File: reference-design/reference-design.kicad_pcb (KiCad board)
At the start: 2 copper layers, 104 x 83.9 mm, 31 parts

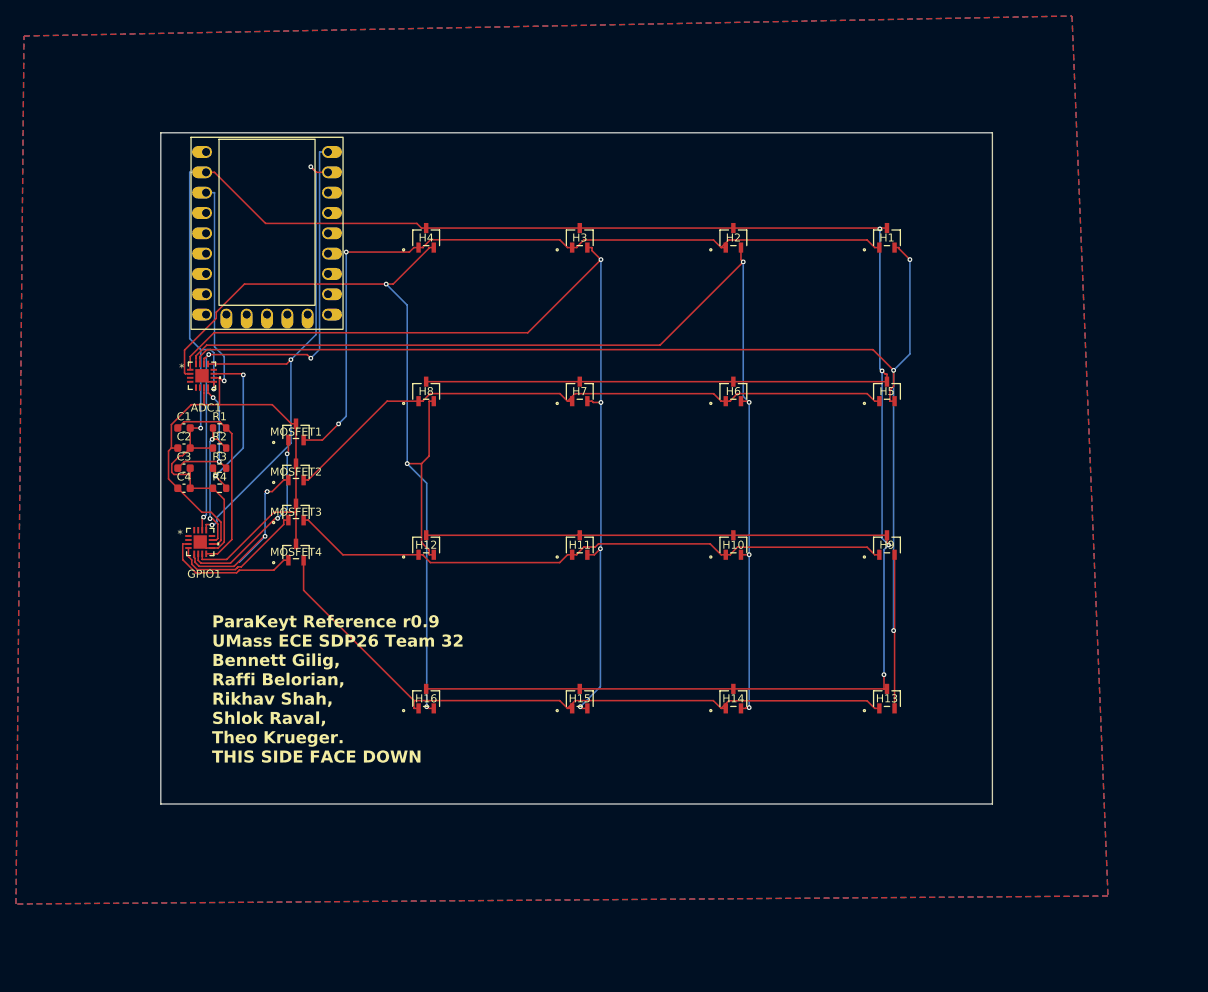
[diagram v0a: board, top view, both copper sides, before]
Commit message: add rp2040 cutout and keyswitch outlines
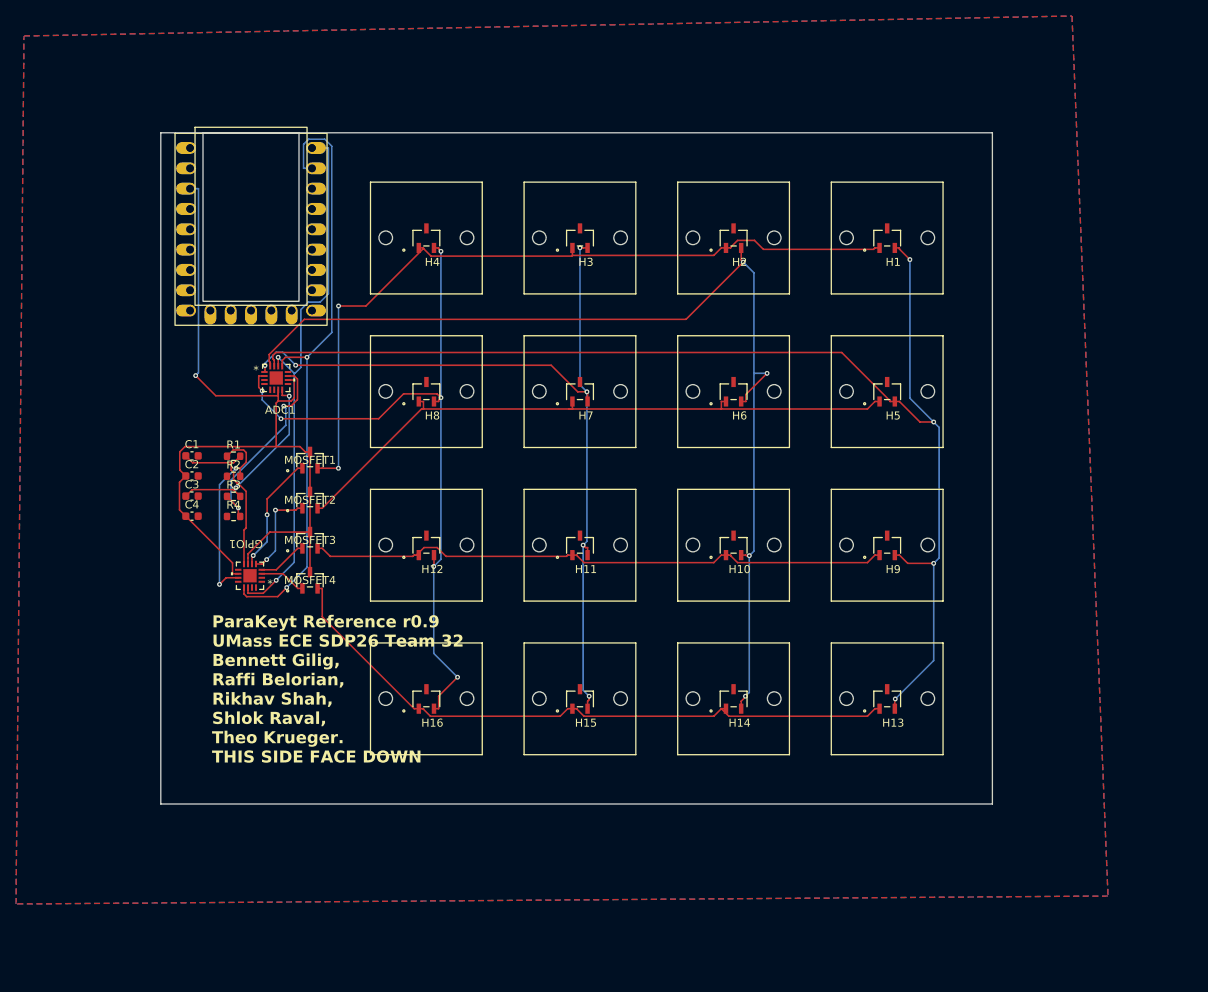
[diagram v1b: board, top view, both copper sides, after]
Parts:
- H1, H10, H11, H12, H13, H14, H15, H16, H2, H3, H4, H5, H6, H7, H8, H9: footprint AH49FNTR_G1:SC59_DIO -> AH49FNTR_G1:SC59_DIO_KeyswitchOutline_NoRuleArea
- moved ADC1 9.28 mm to (26.5, 42.8)
- moved GPIO1 7.52 mm to (23.2, 67.5), turned to 180 degrees
- moved MOSFET4 3.94 mm to (30.8, 68.0)
- moved MOSFET3 3.94 mm to (30.8, 63.0)
- moved R1 3.94 mm to (21.2, 52.5)
- moved R2 3.94 mm to (21.2, 55.0)
- moved R4 3.94 mm to (21.2, 60.1)
- moved MOSFET1 3.94 mm to (30.8, 53.0)
- moved MOSFET2 3.94 mm to (30.8, 58.0)
- moved R3 3.94 mm to (21.2, 57.5)
- moved C1 3.63 mm to (16.0, 52.5)
- moved C2 3.63 mm to (16.0, 55.0)
- moved C4 3.63 mm to (16.0, 60.0)
- moved C3 3.63 mm to (16.0, 57.5)
- moved MCU1 2.06 mm to (23.4, 24.2)
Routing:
- net GND: track 395.8 -> 0.00 mm, vias 6 -> 0
- net col3: track 119.4 -> 92.8 mm, vias 3 -> 6
- net row1: track 30.7 -> 11.7 mm
- net col2: track 122.2 -> 106.4 mm, vias 4 -> 6
- net row3: track 17.3 -> 5.84 mm
- net i2c0_scl: track 65.0 -> 76.4 mm, vias 3 -> 2
- net row2: track 17.6 -> 6.19 mm
- net +3.3V: track 99.7 -> 109.6 mm
- net row0: track 23.6 -> 14.9 mm
- net col0: track 162.9 -> 155.7 mm, vias 3 -> 4
- net Net-(GPIO1-ADDR): track 17.5 -> 24.7 mm
- net Net-(ADC1-DECAP): track 16.6 -> 23.7 mm
- net Net-(H13-VCC): track 86.1 -> 81.5 mm
- net i2c0_sda: track 64.1 -> 68.6 mm, vias 3 -> 2
- net Net-(ADC1-ADDR): track 21.0 -> 25.2 mm
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
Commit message: stfupdate
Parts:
- moved MCU1 2.30 mm to (25.6, 24.7)
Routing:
- net GND: track 0.00 -> 412.4 mm, vias 0 -> 6
- net i2c0_sda: track 68.6 -> 80.7 mm
- net i2c0_scl: track 76.4 -> 64.5 mm
- net col0: track 155.7 -> 145.0 mm, vias 4 -> 2
- net +3.3V: track 109.6 -> 119.2 mm, vias 1 -> 5
- net Net-(H1-VCC): track 96.9 -> 104.8 mm
- net col1: track 132.4 -> 125.7 mm, vias 4 -> 5
- net col2: track 106.4 -> 110.5 mm, vias 6 -> 5
- net row0: track 14.9 -> 18.9 mm
- net Net-(H10-VCC): track 73.6 -> 76.3 mm
- net Net-(GPIO1-ADDR): track 24.7 -> 22.4 mm
- net row1: track 11.7 -> 9.67 mm, vias 2 -> 0
- net col3: track 92.8 -> 91.7 mm, vias 6 -> 4
- net Net-(ADC1-ADDR): track 25.2 -> 24.2 mm
- net Net-(H5-VCC): track 80.2 -> 81.1 mm
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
